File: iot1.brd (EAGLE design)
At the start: 160 x 100 mm, 53 parts, among them IC1 MEGA8-P, IC2 7805T, IC3 LTC2486C, IC4 7805T, IC5 4051N, IC6 OPA2134PA, J1 DCJ0202, U2 HTU21D, X1 22-23-2041, X2 A1944-50

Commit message: rearranging items
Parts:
- moved R14 17.9 mm to (47.2, 75.8)
- moved R12 17.9 mm to (47.1, 83.9)
- moved R13 17.9 mm to (47.1, 79.7)
- moved R15 17.9 mm to (47.4, 71.7)
- moved R16 17.9 mm to (47.4, 67.0)
- moved R17 17.9 mm to (62.5, 83.5)
- moved R18 17.9 mm to (62.5, 79.5)
- moved R19 17.9 mm to (62.6, 75.8)
- moved R20 17.9 mm to (62.6, 71.6)
- moved R21 17.9 mm to (62.8, 67.0)
- moved U1 17.1 mm to (31.4, 70.7)
- moved IC6 10.1 mm to (67.7, 56.9), turned to 180 degrees
- moved U2 9.24 mm to (43.2, 90.3)
- moved C2 5.58 mm to (39.6, 46.9)
- moved R3 5.07 mm to (28.5, 47.0), turned to 0 degrees
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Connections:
- removed net N$43: IC1.4
- removed net N$44: IC1.5
- removed net N$45: IC1.6
- net MUX_0: now also IC1.4
- net MUX_1: now also IC1.5
- net MUX_2: now also IC1.6

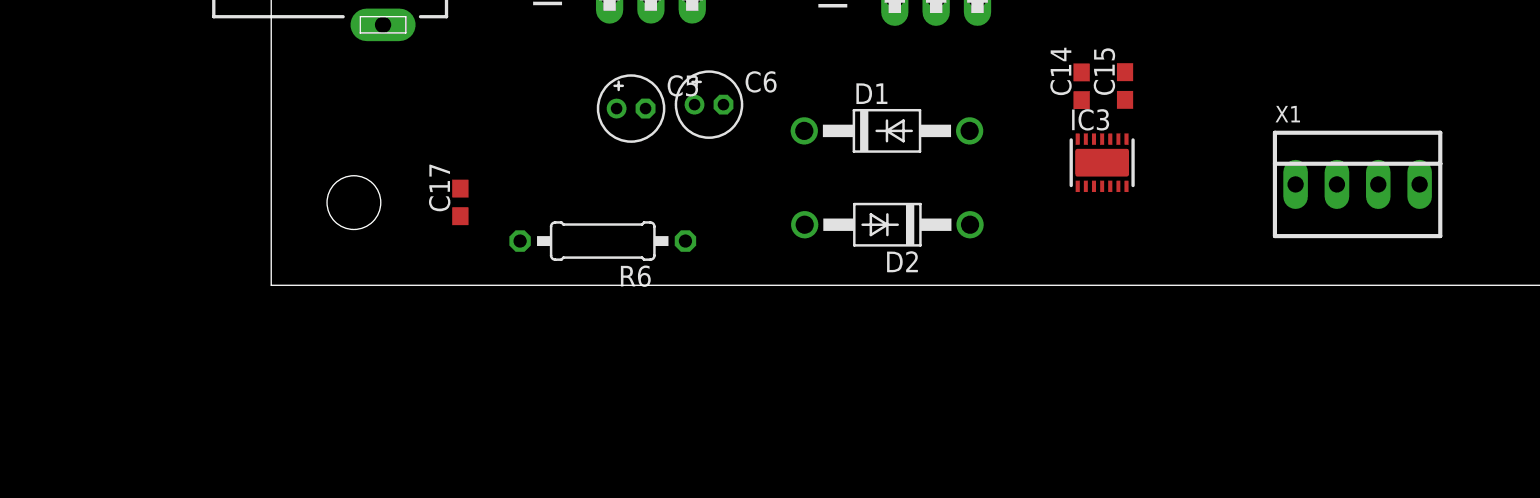
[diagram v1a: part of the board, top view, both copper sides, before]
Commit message: adding MAX485 module
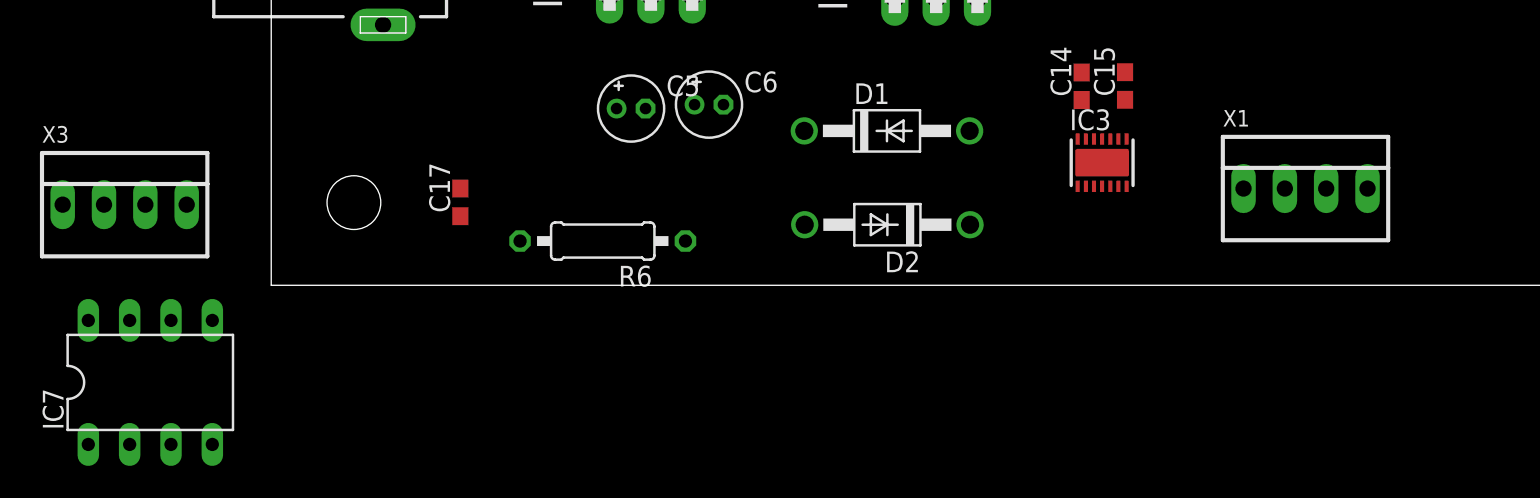
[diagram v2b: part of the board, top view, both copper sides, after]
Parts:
- added IC7: MAX3468CPA, maxim:DIL08
- added X3: 22-23-2041, con-molex:22-23-2041
- moved X1 3.21 mm to (63.6, 5.94)
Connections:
- new net N$43: X3.3
- new net N$44: X3.4
- new net N$7: X3.1
- new net N$8: X3.2
- new net VCC: IC7.8
- net GND: now also IC7.5

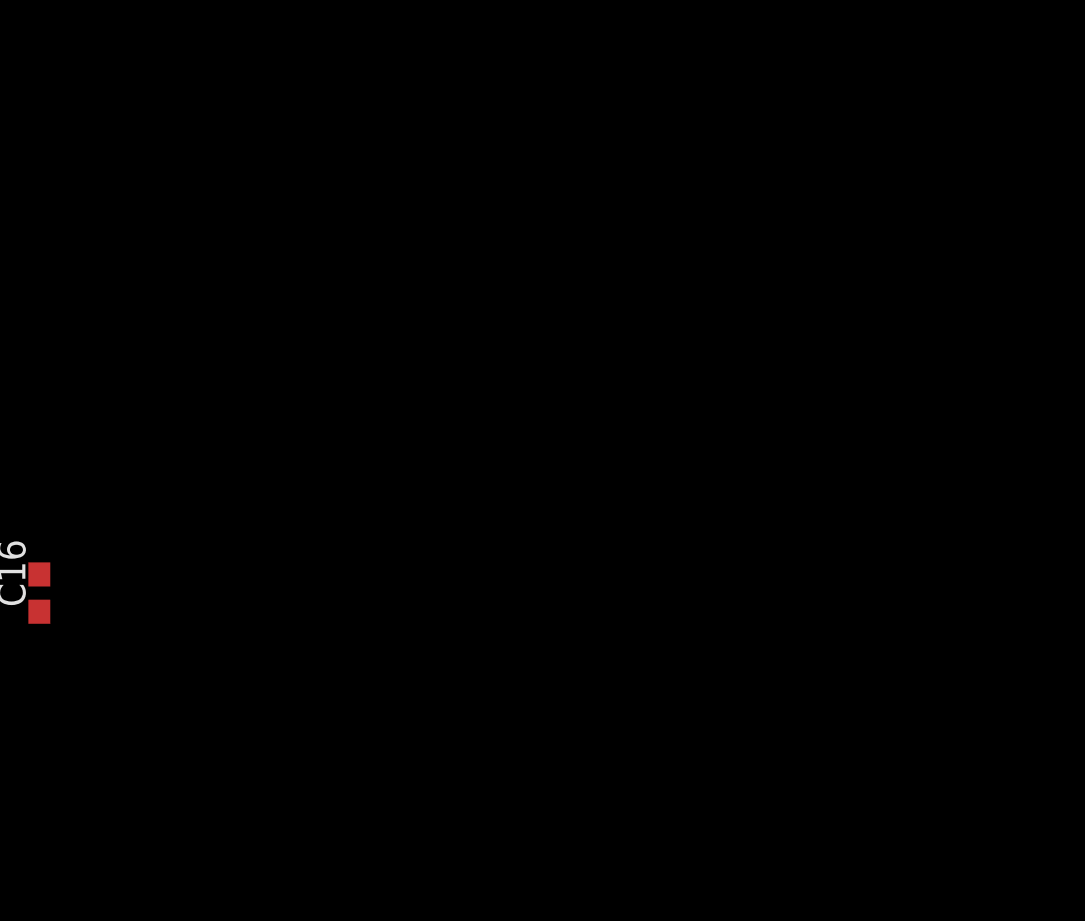
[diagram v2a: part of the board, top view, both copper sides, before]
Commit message: Step-up 5 to 12V
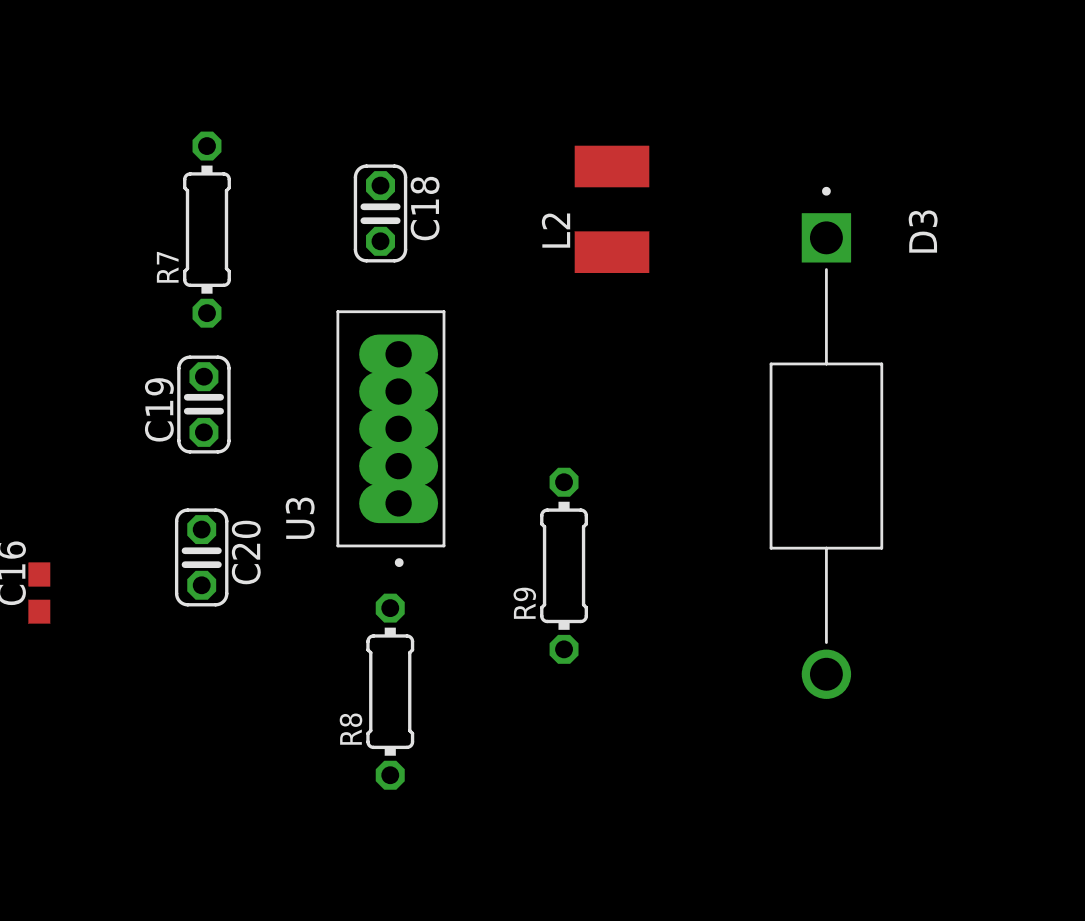
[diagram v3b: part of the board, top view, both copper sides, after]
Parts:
- added C18: 0.1uF, rcl:C025-024X044
- added C19: 0.33uF, rcl:C025-024X044
- added C20: 680uF, rcl:C025-024X044
- added D3: 1N5821, 1N5821:DIOAD1990W125L840D530
- added L2: 100uH, rcl:L1812
- added R7: 2.2k, rcl:0204/7
- added R8: 2k, rcl:0204/7
- added R9: 17.4k, rcl:0204/7
- added U3: LM2577T-ADJ/NOPB, LM2577T-ADJ_NOPB:VREG_LM2577T-ADJ/NOPB
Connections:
- new net 12V: C20.1, D3.1, R9.2
- new net N$45: D3.2, L2.2, U3.4
- new net N$84: R7.2, U3.1
- new net N$85: C19.1, R7.1
- new net N$87: R8.2, R9.1, U3.2
- net 5V: now also C18.1, L2.1, U3.5
- net GND: now also C18.2, C19.2, C20.2, R8.1, U3.3

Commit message: Entrada Sensor de Temperatura y Humedad Ambiente
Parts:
- added X4: 22-23-2041, con-molex:22-23-2041
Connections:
- net 5V: now also X4.3
- net GND: now also X4.4
- net SCL: now also X4.2
- net SDA: now also X4.1

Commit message: LED
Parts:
- added LED1: (no value), led:LED3MM
- added R10: 680, rcl:0207/10
- added STANDOFF3, STANDOFF4: STAND-OFF, SparkFun-Electromechanical:STAND-OFF
- moved STANDOFF1 0.69 mm to (4.45, 95.0)
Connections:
- new net N$76: LED1.K, R10.2
- net GND: now also R10.1
- net N$15: now also LED1.A
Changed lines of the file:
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@@
 <attribute name="VALUE" x="22.4028" y="89.3699" size="0.4064" layer="27"/>
 </element>
-<element name="STANDOFF1" library="SparkFun-Electromechanical" package="STAND-OFF" value="STAND-OFF" x="3.81" y="95.25" smashed="yes"/>
+<element name="STANDOFF1" library="SparkFun-Electromechanical" package="STAND-OFF" value="STAND-OFF" x="4.445" y="94.9833" smashed="yes"/>
 <element name="STANDOFF2" library="SparkFun-Electromechanical" package="STAND-OFF" value="STAND-OFF" x="5.08" y="5.08" smashed="yes"/>
 <element name="U1" library="FaBo-LoRa" package="CMWX1ZZABZ" value="" x="31.4452" y="70.7136" smashed="yes" rot="R180">
@@
 <attribute name="VALUE" x="77.5843" y="0.8763" size="1.016" layer="27" ratio="10"/>
 </element>
+<element name="LED1" library="led" library_urn="urn:adsk.eagle:library:259" package="LED3MM" package3d_urn="urn:adsk.eagle:package:15797/1" value="" x="76.0984" y="77.4319" smashed="yes">
+<attribute name="NAME" x="78.0034" y="77.8129" size="1.27" layer="25" ratio="10"/>
+<attribute name="POPULARITY" value="97" x="76.0984" y="77.4319" size="1.778" layer="27" display="off"/>
+<attribute name="VALUE" x="78.0034" y="75.7809" size="1.27" layer="27" ratio="10"/>
+</element>
+<element name="R10" library="rcl" library_urn="urn:adsk.eagle:library:334" package="0207/10" package3d_urn="urn:adsk.eagle:package:23491/2" value="680" x="76.2381" y="83.8708" smashed="yes">
+<attribute name="NAME" x="73.1901" y="85.3948" size="1.27" layer="25" ratio="10"/>
+<attribute name="POPULARITY" value="81" x="76.2381" y="83.8708" size="1.778" layer="27" display="off"/>
+<attribute name="SPICEPREFIX" value="R" x="76.2381" y="83.8708" size="1.778" layer="27" display="off"/>
+<attribute name="VALUE" x="73.9775" y="83.2358" size="1.27" layer="27" ratio="10"/>
+</element>
+<element name="STANDOFF3" library="SparkFun-Electromechanical" package="STAND-OFF" value="STAND-OFF" x="154.0256" y="94.0181" smashed="yes"/>
+<element name="STANDOFF4" library="SparkFun-Electromechanical" package="STAND-OFF" value="STAND-OFF" x="154.8765" y="4.8006" smashed="yes"/>
 </elements>
 <signals>
@@
 <contactref element="C20" pad="2"/>
 <contactref element="X4" pad="4"/>
+<contactref element="R10" pad="1"/>
 <wire x1="92.6973" y1="51.7489" x2="91.8718" y2="60.2996" width="0" layer="19" extent="1-1"/>
 <wire x1="83.82" y1="54.1274" x2="92.6973" y2="51.7489" width="0" layer="19" extent="1-1"/>
@@
 <wire x1="57.0103" y1="30.8483" x2="50.7238" y2="30.4927" width="0" layer="19" extent="1-1"/>
 <wire x1="-3.6195" y1="-2.159" x2="11.6205" y2="5.9427" width="0" layer="19" extent="1-1"/>
-<wire x1="86.4743" y1="5.9563" x2="-3.6195" y2="-2.159" width="0" layer="19" extent="1-1"/>
+<wire x1="86.4743" y1="5.9563" x2="67.3608" y2="5.9436" width="0" layer="19" extent="1-1"/>
+<wire x1="71.1581" y1="83.8708" x2="-3.6195" y2="-2.159" width="0" layer="19" extent="1-1"/>
 </signal>
 <signal name="SCL">
@@
 <signal name="N$15">
 <contactref element="IC1" pad="23"/>
+<contactref element="LED1" pad="A"/>
+<wire x1="74.8284" y1="77.4319" x2="37.338" y2="60.6044" width="0" layer="19" extent="1-1"/>
 </signal>
 <signal name="N$16">
@@
 <wire x1="92.6973" y1="50.0489" x2="100.2411" y2="41.6941" width="0" layer="19" extent="1-1"/>
 </signal>
+<signal name="N$76">
+<contactref element="LED1" pad="K"/>
+<contactref element="R10" pad="2"/>
+<wire x1="81.3181" y1="83.8708" x2="77.3684" y2="77.4319" width="0" layer="19" extent="1-1"/>
+</signal>
 </signals>

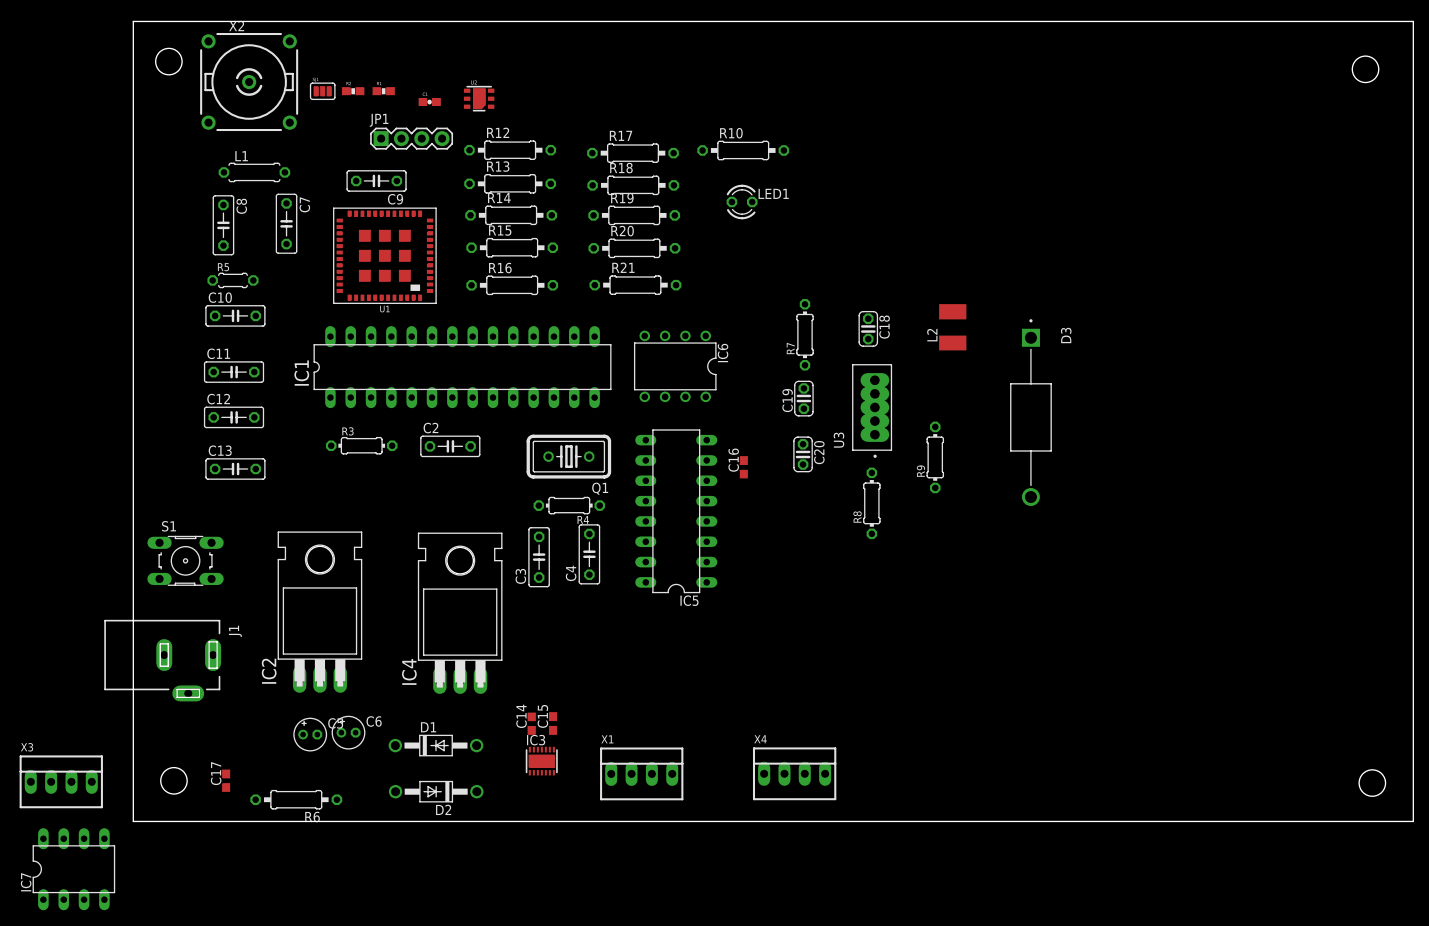
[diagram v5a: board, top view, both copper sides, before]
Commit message: adding MAX3468
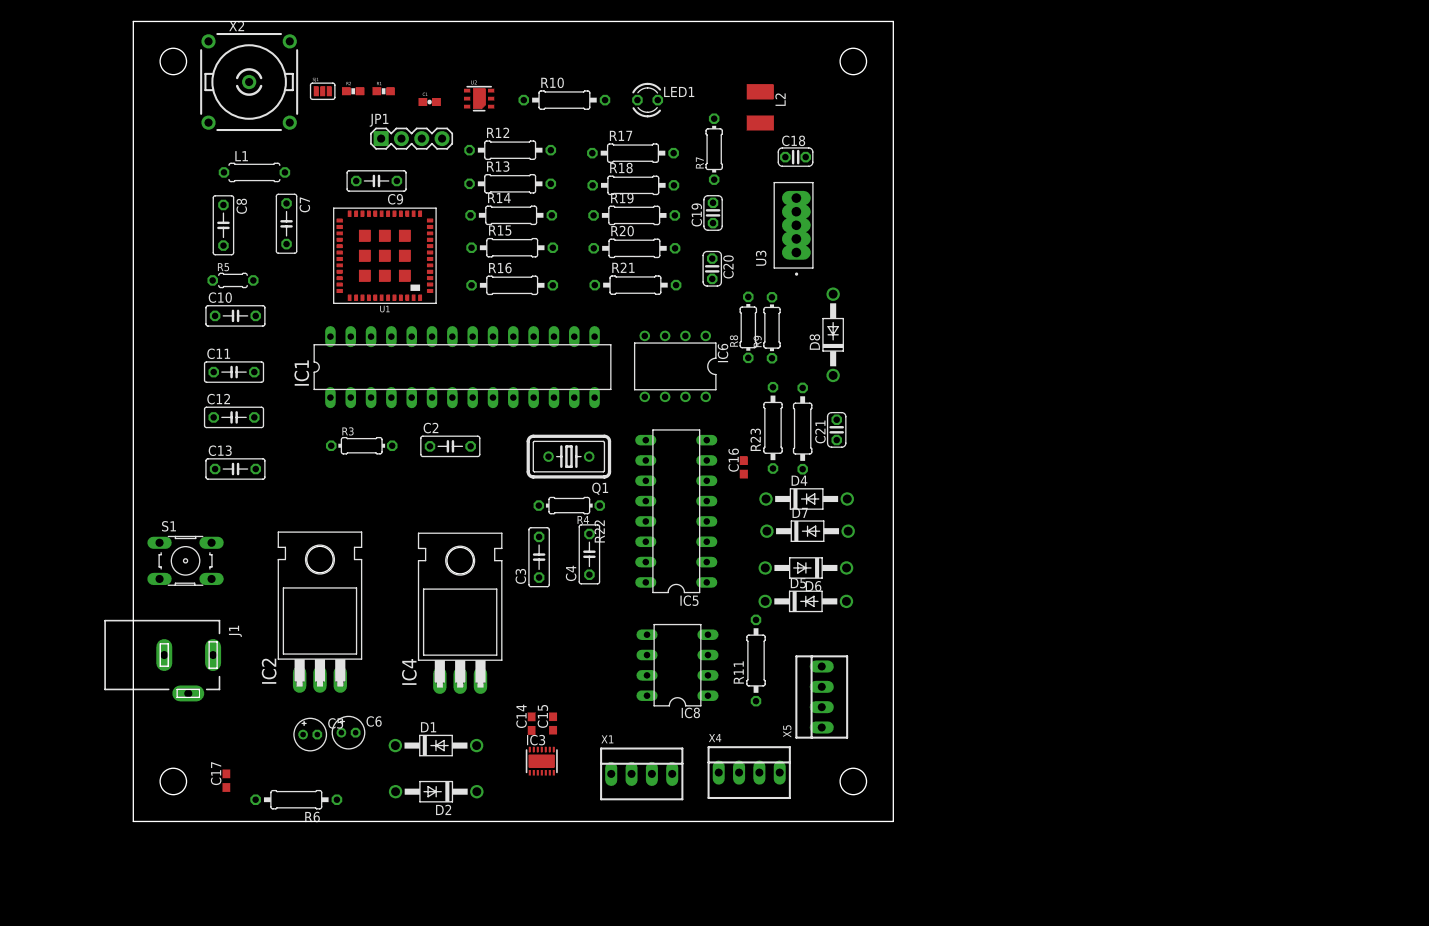
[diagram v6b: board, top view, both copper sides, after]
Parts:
- removed D3: 1N5821, 1N5821:DIOAD1990W125L840D530
- removed IC7: MAX3468CPA, maxim:DIL08
- removed X3: 22-23-2041, con-molex:22-23-2041
- added C21: (no value), rcl:C025-024X044
- added D4, D5, D6, D7, D8: 1N4004, diode:DO41-10
- added IC8: MAX3468CPA, maxim:DIL08
- added R11, R22, R23: (no value), rcl:0207/10
- added X5: 22-23-2041, con-molex:22-23-2041
- moved STANDOFF4 64.9 mm to (90.0, 5.00)
- moved STANDOFF3 64.0 mm to (90.0, 95.0)
- moved L2 36.5 mm to (78.4, 89.3), turned to 270 degrees
- moved R8 26.9 mm to (76.9, 61.8)
- moved R9 26.1 mm to (79.8, 61.7)
- moved C19 25.8 mm to (72.5, 76.1)
- moved R7 25.8 mm to (72.6, 84.0)
- moved C20 25.8 mm to (72.4, 69.1)
- moved U3 24.8 mm to (82.9, 71.1)
- moved C18 23.3 mm to (82.8, 83.0), turned to 0 degrees
- moved R10 23.2 mm to (53.9, 90.2)
- moved LED1 17.4 mm to (64.3, 90.2)
- moved X4 5.68 mm to (77.0, 6.11)
- moved STANDOFF1 0.56 mm to (5.00, 95.0)
- moved STANDOFF2 0.11 mm to (5.00, 5.00)
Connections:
- removed net N$23: IC1.26
- removed net N$43: X3.3
- removed net N$44: X3.4
- removed net N$7: X3.1
- removed net N$8: X3.2
- removed net VCC: IC7.8
- new net 485A: D6.C, D7.A, IC8.6, R11.1, R22.2, X5.3
- new net 485B: D4.A, D5.C, IC8.7, R11.2, R23.1, X5.4
- new net N$88: IC8.4
- new net TX_485: IC1.26, IC8.1
- net 12V: now also D8.C, X5.1; no longer D3.1
- net 3.3V: now also C21.1, IC8.8, R22.1
- net 5V: now also D4.C, D7.C
- net GND: now also C21.2, D5.A, D6.A, IC8.2, IC8.3, IC8.5, R23.2, X5.2; no longer IC7.5
- net N$45: now also D8.A; no longer D3.2
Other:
- board size 160 x 100 mm -> 95 x 100 mm

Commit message: adding important wires
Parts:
- moved IC8 1.09 mm to (68.4, 18.5)
- moved C4 0.34 mm to (57.0, 33.0)
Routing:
- net 5V: track 0.00 -> 309.8 mm
- net 3.3V: track 0.00 -> 195.8 mm
- net 12V: track 0.00 -> 69.2 mm
- net RF_LORAWAN: track 0.00 -> 25.4 mm
- net N$72: track 0.00 -> 24.2 mm
- net N$73: track 0.00 -> 20.8 mm
- net V_IN: track 0.00 -> 19.2 mm
- net N$45: track 0.00 -> 13.9 mm

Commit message: all conections
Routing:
- net GND: track 0.00 -> 631.6 mm
- net SCL: track 0.00 -> 192.2 mm, vias 0 -> 2
- net SDA: track 0.00 -> 177.8 mm
- net SOIL_MOISTURE_0: track 0.00 -> 136.1 mm
- net SOIL_MOISTURE_1: track 0.00 -> 124.2 mm
- net TX_485: track 0.00 -> 98.2 mm
- net 485A: track 0.00 -> 74.0 mm
- net S: track 0.00 -> 69.8 mm
- net SOIL_MOISTURE_AMPLIFIED_0: track 0.00 -> 67.6 mm
- net 485B: track 0.00 -> 66.3 mm
- net SOIL_MOISTURE_AMPLIFIED_1: track 0.00 -> 54.7 mm
- net N$15: track 0.00 -> 50.2 mm
- net SENSORS: track 0.00 -> 47.7 mm
- net N$38: track 0.00 -> 44.4 mm, vias 0 -> 1
- net N$78: track 0.00 -> 37.9 mm
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- added copper zone on layer 1, net GND
- added copper zone on layer 16, net GND
